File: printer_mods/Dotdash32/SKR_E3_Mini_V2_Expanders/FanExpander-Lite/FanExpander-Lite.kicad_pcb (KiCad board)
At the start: 2 copper layers, 30.9 x 27.9 mm, 34 parts, among them J1 JST-XH2, J2 JST-XH2, J3 JST-XH2, J4 JST-XH2, J5 EXP1_IN, J6 JST-XH2, J7 IO_PassThrough, Q1 IRLML6344, Q2 IRLML6344, Q3 IRLML6344

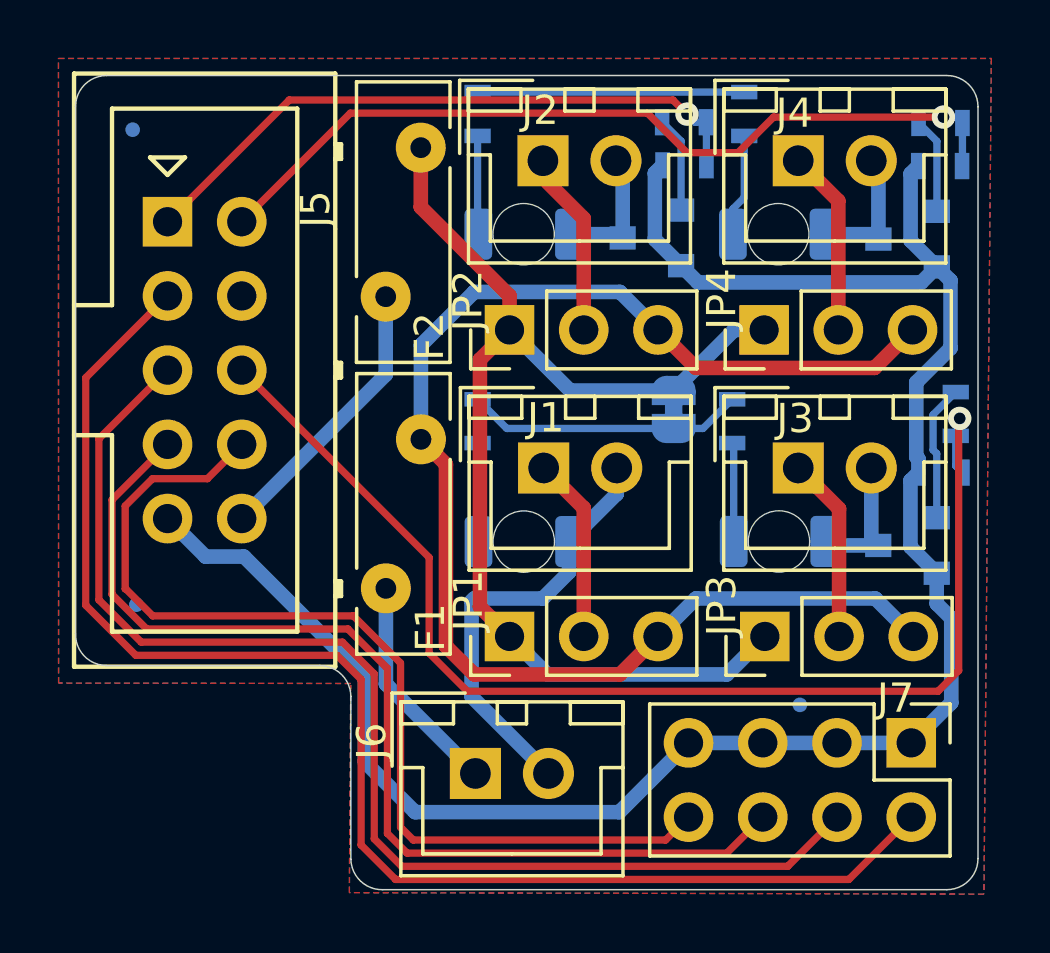
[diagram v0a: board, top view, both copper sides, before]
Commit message: feat: solder paste filled jumpers
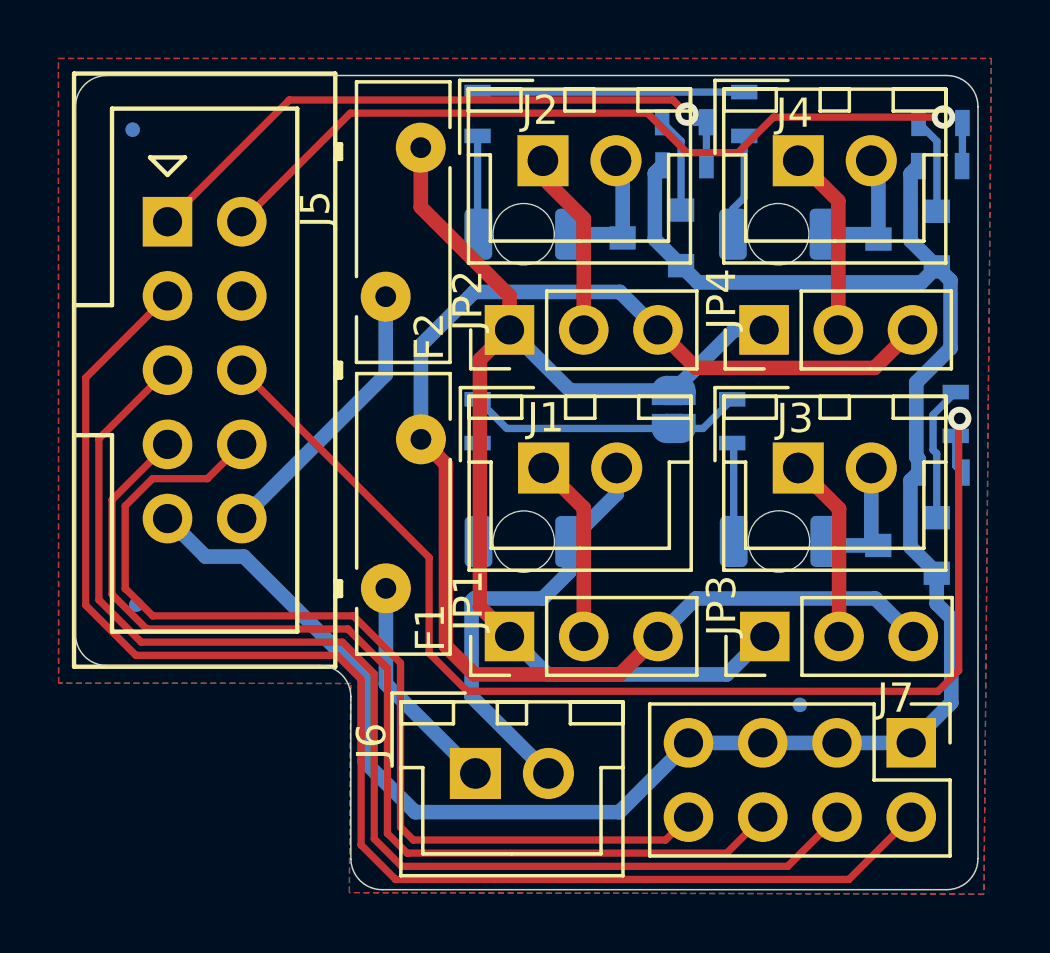
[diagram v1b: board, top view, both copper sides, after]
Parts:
- JP5: footprint Jumper:SolderJumper-2_P1.3mm_Bridged_RoundedPad1.0x1.5mm -> Jumper:SolderJumper-2_P1.3mm_Pasted_RoundedPad1.0x1.5mm
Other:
- board text added: "by Dotdash32 (JDeW) V1.0.4"
- board text removed: "by Dotdash32 (JDeW) V1.0.3"

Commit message: chore: update to KiCad 6.0, better EXP 3D model
move to KiCad 6 in order to export step files, lol.
Also, improve the direct EXP1 plug in so it's more accurate to size

add local .gitignore to ignore backup files
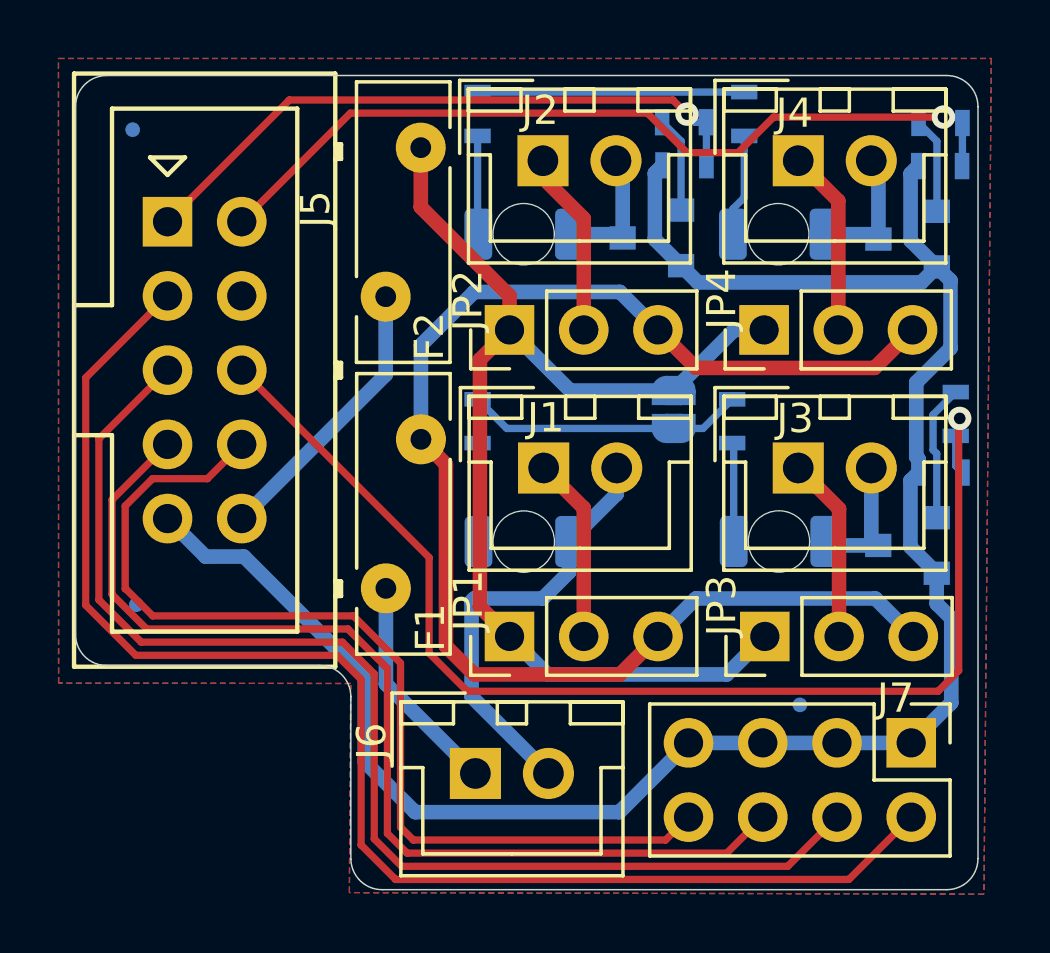
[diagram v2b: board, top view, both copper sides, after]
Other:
- net class Default removed
- net class Power removed
